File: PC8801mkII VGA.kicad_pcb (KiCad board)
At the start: 2 copper layers, 40.6 x 24.1 mm, 5 parts

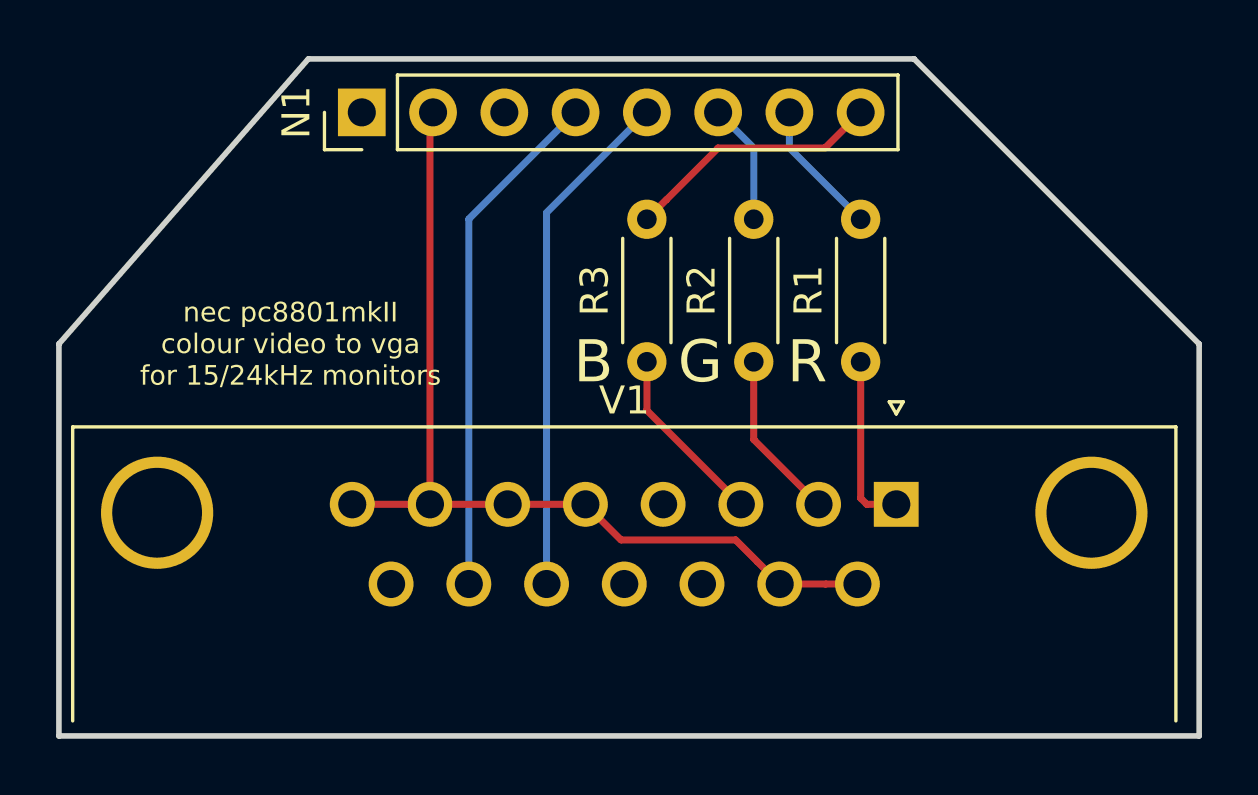
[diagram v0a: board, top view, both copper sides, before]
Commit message: Use the 3-row right angle VGA connector which is all digikey seems to have
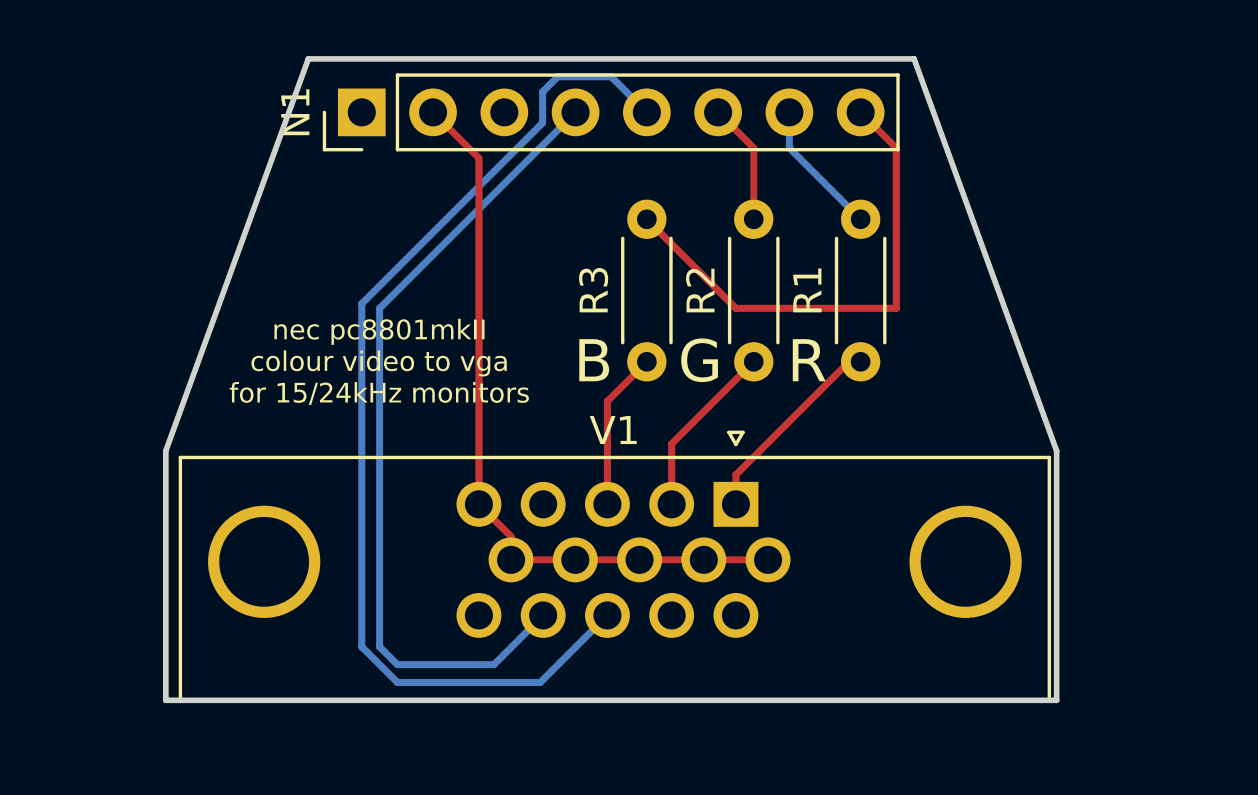
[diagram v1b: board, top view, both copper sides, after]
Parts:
- V1: footprint Connector_Dsub:DSUB-15_Female_Horizontal_P2.77x2.84mm_EdgePinOffset4.94mm_Housed_MountingHolesOffset7.48mm -> Connector_Dsub:DSUB-15-HD_Female_Horizontal_P2.29x1.98mm_EdgePinOffset3.03mm_Housed_MountingHolesOffset4.94mm
- moved V1 5.72 mm to (156.2, 107.3)
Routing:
- net /H-Sync: track 18.3 -> 37.2 mm
- net /V-Sync: track 18.4 -> 28.8 mm
- net /Blue: track 15.7 -> 23.4 mm
- net /GND: track 33.2 -> 26.4 mm
- net /Red: track 11.1 -> 12.0 mm
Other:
- board size 40.6 x 24.1 mm -> 31.8 x 22.9 mm

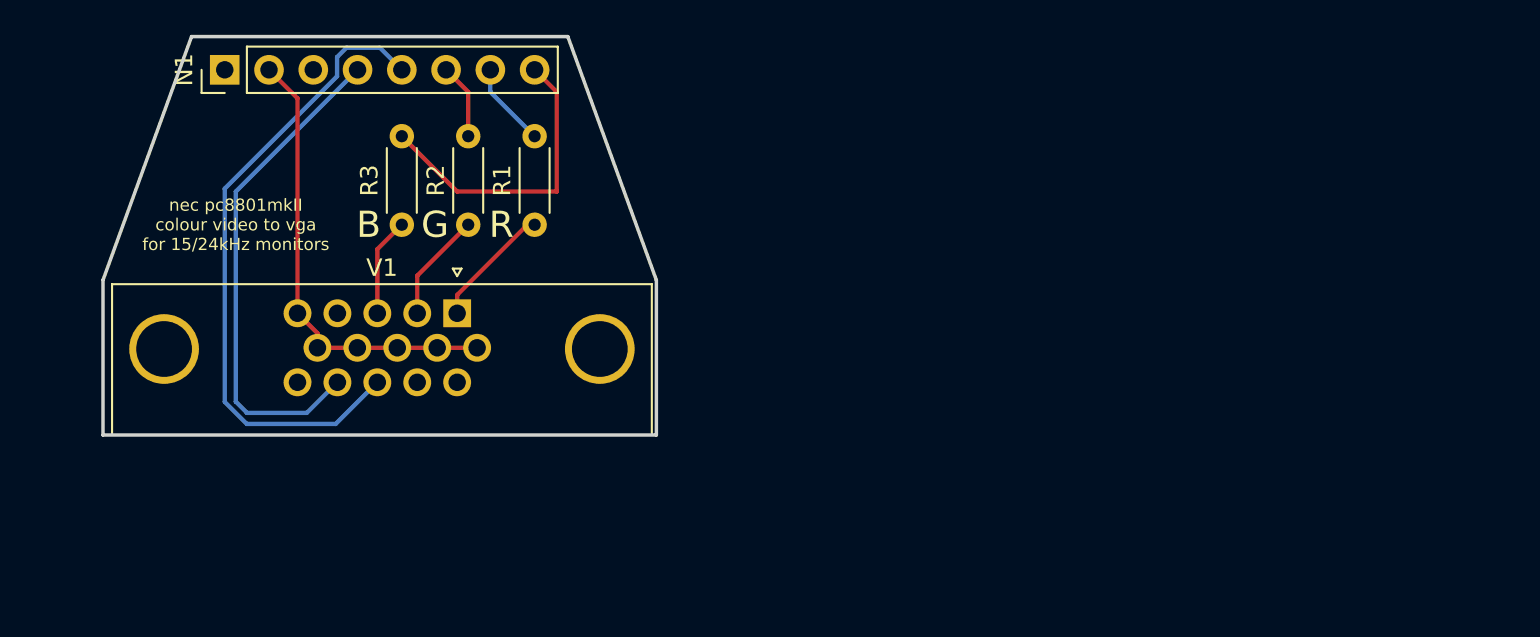
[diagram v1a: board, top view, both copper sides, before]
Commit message: Revision with ACTUAL PARTS
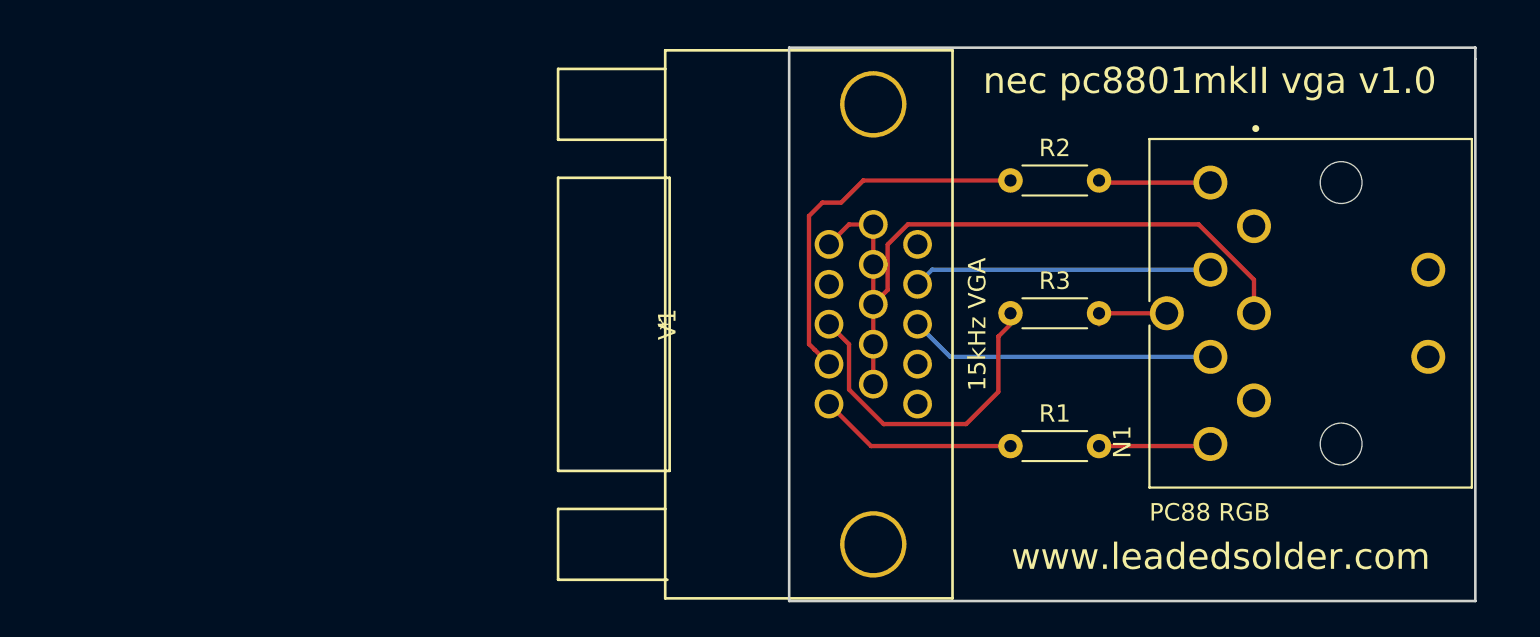
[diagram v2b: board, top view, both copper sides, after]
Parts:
- N1: footprint Pin_Headers:Pin_Header_Straight_1x08_Pitch2.54mm -> SDS-80J:CUI_SDS-80J
- V1: footprint Connector_Dsub:DSUB-15-HD_Female_Horizontal_P2.29x1.98mm_EdgePinOffset3.03mm_Housed_MountingHolesOffset4.94mm -> Connector_TE_AMP_HD15:1-1734530-1
- moved N1 60.7 mm to (201.9, 107.3)
- moved R3 35.3 mm to (188.0, 107.3), turned to 0 degrees
- moved R2 31.2 mm to (188.0, 99.7), turned to 0 degrees
- moved R1 30.1 mm to (188.0, 114.9), turned to 0 degrees
- moved V1 12.1 mm to (168.3, 108.0), turned to 90 degrees
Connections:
- R1 pad 1: /Red -> /Red_VGA
- R2 pad 1: /Green -> /Green_VGA
- R3 pad 1: /Blue -> /Blue_VGA
- V1 pad 1: /Red -> /Red_VGA
- V1 pad 2: /Green -> /Green_VGA
- V1 pad 3: /Blue -> /Blue_VGA
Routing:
- net /Green_VGA: track 0.00 -> 21.4 mm
- net /H-Sync: track 37.2 -> 17.6 mm
- net /Blue: track 23.4 -> 4.15 mm
- net /Blue_VGA: track 0.00 -> 18.5 mm
- net /GND: track 26.4 -> 40.7 mm
- net /V-Sync: track 28.8 -> 17.2 mm
- net /Red_VGA: track 0.00 -> 11.4 mm
- net /Red: track 12.0 -> 6.44 mm
- net /Green: track 10.6 -> 6.44 mm
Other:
- board size 31.8 x 22.9 mm -> 39.4 x 31.8 mm
- board text added: "nec pc8801mkII vga v1.0"
- board text removed: "12V"
- board text removed: "B"
- board text removed: "Blue"
- board text removed: "G"
- board text removed: "GND"
- board text removed: "Green"
- board text removed: "H-Sync"
- board text removed: "R"
- board text removed: "Red"
- board text removed: "V-Sync"
- board text removed: "nec pc8801mkII colour video to vga for 15/24kHz monitors"

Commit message: Revised schematic based on the female pinout
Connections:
- N1 pad 1: Net-(N1-Pad1) -> /12V
- N1 pad 3: /12V -> /NC
- N1 pad 4: /V-Sync -> /H-Sync
- N1 pad 5: /H-Sync -> /V-Sync
- N1 pad 6: /Green -> /Red
- N1 pad 7: /Red -> /Green
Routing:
- net /Red: track 6.44 -> 28.2 mm
- net /Green: track 6.44 -> 23.8 mm
- net /V-Sync: track 17.2 -> 27.9 mm
- net /H-Sync: track 17.6 -> 18.1 mm

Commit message: Add pointless silkscreen
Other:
- board text added: "150Ω resistors"
- board text added: "use with 15/24kHz vga monitor"
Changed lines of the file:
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@@
   (general
     (thickness 1.6)
-    (drawings 7)
+    (drawings 9)
     (tracks 52)
     (zones 0)
@@
     (pad Hole np_thru_hole circle (at 7.5 5 90) (size 2.4 2.4) (drill 2.4) (layers *.Cu *.Mask F.SilkS))
   )
+  (gr_text "150Ω resistors" (at 198.12 93.98) (layer B.SilkS)
+    (effects (font (size 1.5 1.5) (thickness 0.3)) (justify mirror))
+  )
+  (gr_text "use with 15/24kHz vga monitor" (at 194.945 117.475) (layer B.SilkS)
+    (effects (font (size 1.5 1.5) (thickness 0.3)) (justify mirror))
+  )
   (gr_text "nec pc8801mkII vga v1.0" (at 199.39 93.98) (layer F.SilkS)

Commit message: Label resistors
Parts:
- renumbered R3 to Blue, R2 to Green, R1 to Red
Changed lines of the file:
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@@
     (descr "Resistor, Axial_DIN0204 series, Axial, Horizontal, pin pitch=5.08mm, 0.16666666666666666W = 1/6W, length*diameter=3.6*1.6mm^2, http://cdn-reichelt.de/documents/datenblatt/B400/1_4W%23YAG.pdf")
     (tags "Resistor Axial_DIN0204 series Axial Horizontal pin pitch 5.08mm 0.16666666666666666W = 1/6W length 3.6mm diameter 1.6mm")
-    (fp_text reference R3 (at 2.54 -1.86) (layer F.SilkS)
+    (fp_text reference Blue (at 2.54 -1.86) (layer F.SilkS)
       (effects (font (size 1 1) (thickness 0.15)))
     )
@@
     (descr "Resistor, Axial_DIN0204 series, Axial, Horizontal, pin pitch=5.08mm, 0.16666666666666666W = 1/6W, length*diameter=3.6*1.6mm^2, http://cdn-reichelt.de/documents/datenblatt/B400/1_4W%23YAG.pdf")
     (tags "Resistor Axial_DIN0204 series Axial Horizontal pin pitch 5.08mm 0.16666666666666666W = 1/6W length 3.6mm diameter 1.6mm")
-    (fp_text reference R2 (at 2.54 -1.86) (layer F.SilkS)
+    (fp_text reference Green (at 2.54 -1.86) (layer F.SilkS)
       (effects (font (size 1 1) (thickness 0.15)))
     )
@@
     (descr "Resistor, Axial_DIN0204 series, Axial, Horizontal, pin pitch=5.08mm, 0.16666666666666666W = 1/6W, length*diameter=3.6*1.6mm^2, http://cdn-reichelt.de/documents/datenblatt/B400/1_4W%23YAG.pdf")
     (tags "Resistor Axial_DIN0204 series Axial Horizontal pin pitch 5.08mm 0.16666666666666666W = 1/6W length 3.6mm diameter 1.6mm")
-    (fp_text reference R1 (at 2.54 -1.86) (layer F.SilkS)
+    (fp_text reference Red (at 2.54 -1.86) (layer F.SilkS)
       (effects (font (size 1 1) (thickness 0.15)))
     )

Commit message: Revised footprint
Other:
- board text added: "nec pc8801mkII vga v1.1"
- board text removed: "nec pc8801mkII vga v1.0"
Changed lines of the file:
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@@
     (effects (font (size 1.5 1.5) (thickness 0.3)) (justify mirror))
   )
-  (gr_text "nec pc8801mkII vga v1.0" (at 199.39 93.98) (layer F.SilkS)
+  (gr_text "nec pc8801mkII vga v1.1" (at 199.39 93.98) (layer F.SilkS)
     (effects (font (size 1.5 1.5) (thickness 0.3)))
   )

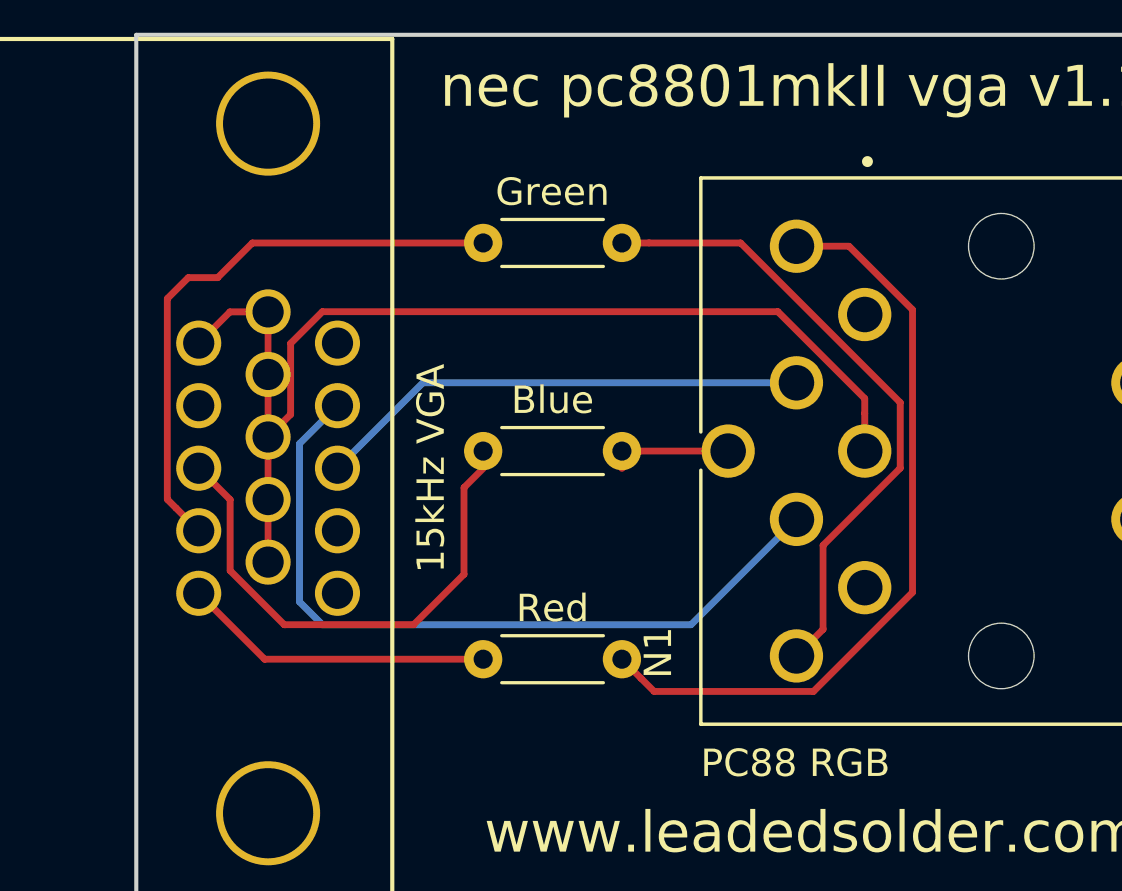
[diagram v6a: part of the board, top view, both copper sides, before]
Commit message: Flipped version using fixed footprint
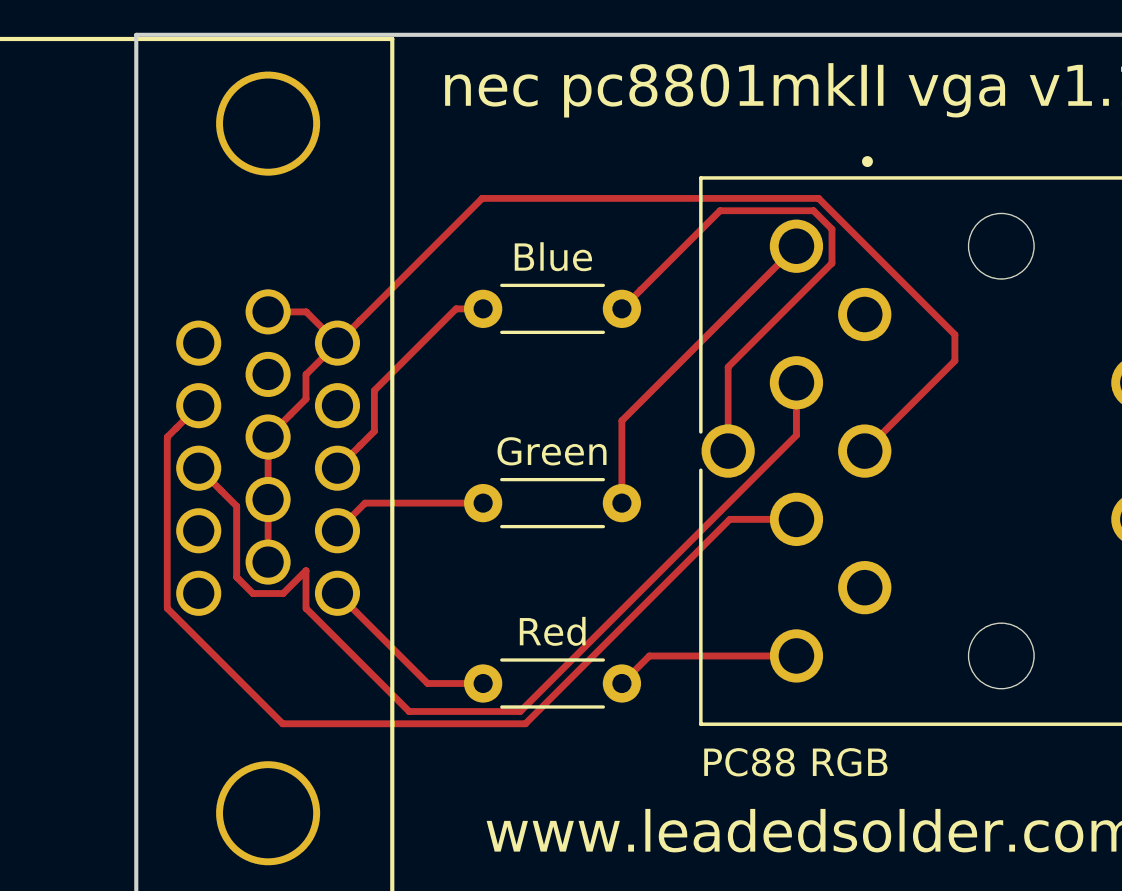
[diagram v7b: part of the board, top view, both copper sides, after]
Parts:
- V1: footprint Connector_TE_AMP_HD15:1-1734530-1 -> Connector_TE_AMP_HD15:FIXED-1-1734530-1
- moved Green 9.53 mm to (188.0, 109.2)
- moved Blue 5.21 mm to (188.0, 102.1)
- moved Red 0.89 mm to (188.0, 115.8)
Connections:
- N1 pad 4: /H-Sync -> /V-Sync
- N1 pad 5: /V-Sync -> /H-Sync
- N1 pad 6: /Red -> /Green
- N1 pad 7: /Green -> /Red
- V1 pad 13: /H-Sync -> /V-Sync
- V1 pad 14: /V-Sync -> /H-Sync
- V1 pad 9: /GND -> /KEY
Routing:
- net /Red: track 28.2 -> 6.98 mm
- net /H-Sync: track 18.1 -> 35.8 mm
- net /Green_VGA: track 21.4 -> 5.75 mm
- net /Blue: track 4.15 -> 19.2 mm
- net /Green: track 23.8 -> 12.1 mm
- net /Blue_VGA: track 18.5 -> 8.62 mm
- net /V-Sync: track 27.9 -> 34.7 mm
- net /Red_VGA: track 11.4 -> 6.70 mm
- net /GND: track 40.7 -> 44.6 mm
